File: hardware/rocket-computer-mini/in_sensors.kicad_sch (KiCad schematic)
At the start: 17 parts, among them J1 BM05B-SRSS-TB, U2 ISM6HG256XTR, U27 TPS22810DRVR, U3 IIS2MDCTR, U4 BMP585

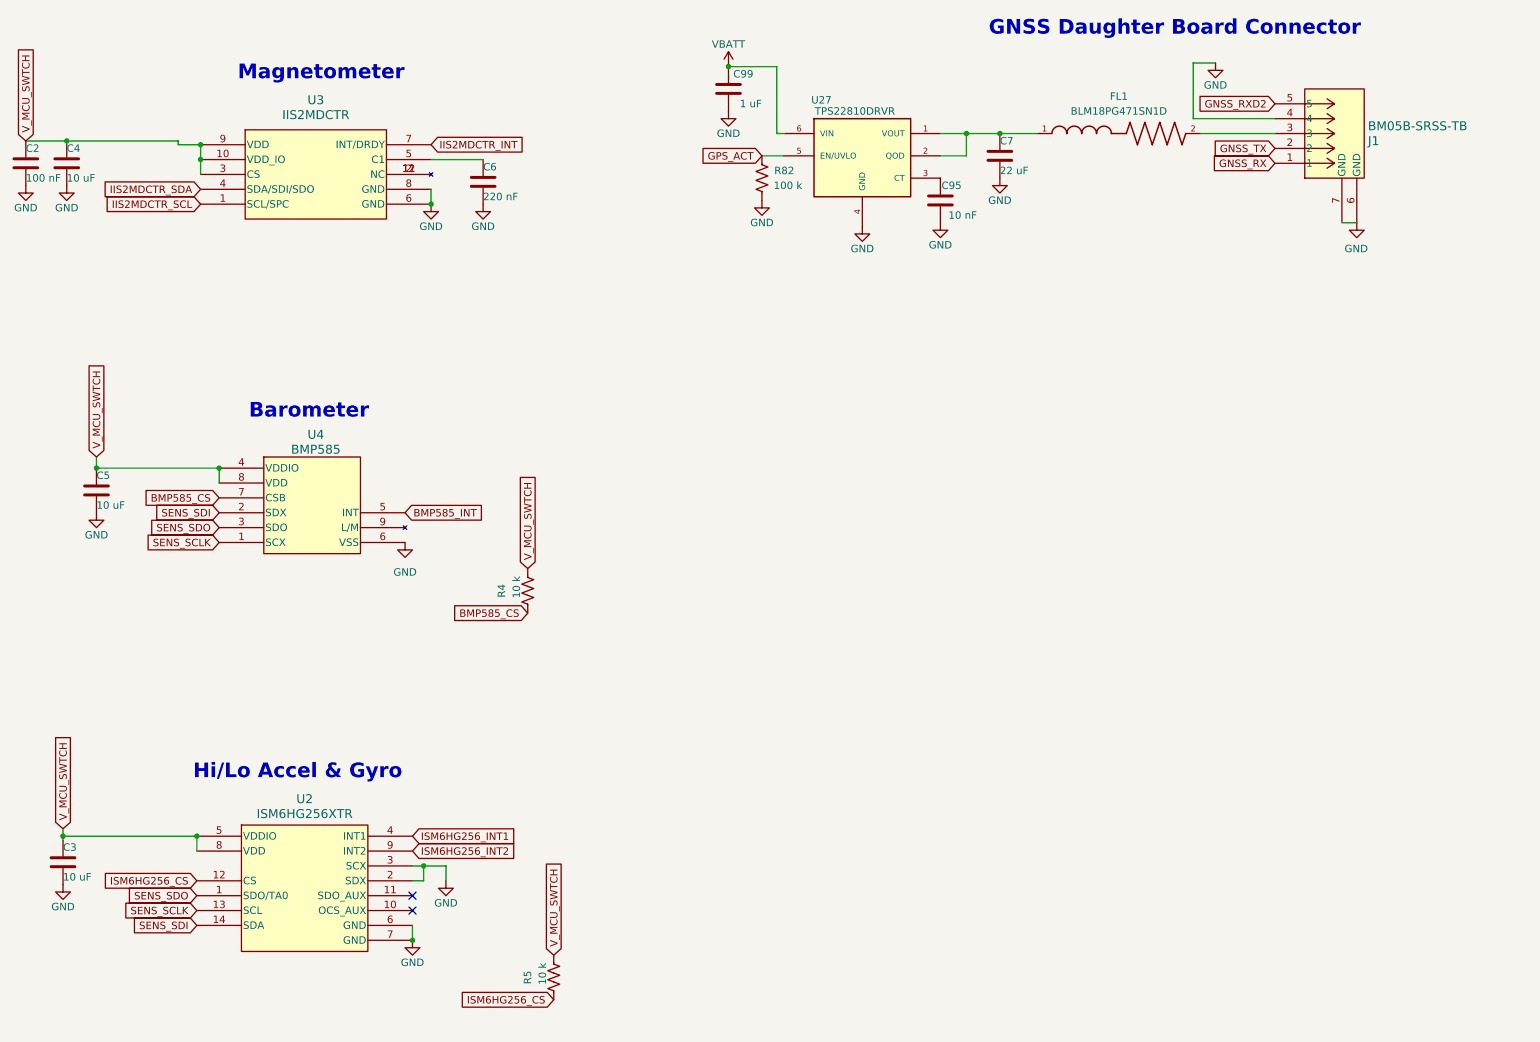
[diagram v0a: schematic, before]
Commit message: hardware: rocket-computer-mini gains the on-board radio, sheds more parts
Second reduction pass, plus the radio moves on-board.

Added: the 900 MHz radio module (U16) and its two decoupling caps, wired for
direct SPI rather than through the daughterboard connector. Removed: 31
designators including the camera connector (J4), the piezo (LS1), mounting
hardware (H5-H8), and the support parts that went with them. Also gone are the
magnetometer interrupt and the inertial sensor's second interrupt -- neither was
ever used by firmware, which is what made them free to drop.

Parts 190 -> 161, nets 191 -> 165.

Adds a pin budget for the reduced board (pin-budget.md). The headline is that
the board fits, but not comfortably: 23 signals against 27 usable pads, and only
16 of those pads are free of strapping, console, JTAG or flash-adjacent duty.

Three findings shaped it:

- The radio needs seven pins, not nine. DIO2 drives transmit-enable inside the
  module and needs no processor pin; receive-enable is floating and has no
  firmware pin at all. The out-computer firmware still carries the direct-SPI
  driver from the V7 topology and defines exactly those seven, so putting the
  bare module back on-board is a board change rather than a firmware rewrite.
- Pyro continuity is a digital read, not analogue, and nothing on this board
  needs an ADC channel -- so the ADC2-versus-radio restriction does not
  constrain the design.
- Continuity belongs on an I2C expander, not a multiplexer. A four-to-one mux
  needs two select lines plus data, saving one pin; the expander shares the bus
  the magnetometer is joining and saves four.

The proposed assignment keeps the serial console free and spends JTAG. Pyro
firing is confined to unrestricted pins -- never a strapping pin and never one
the boot ROM drives, since the console transmit pin is active on every boot.

One assumption can invalidate it: three signals sit on flash-adjacent pads that
are free only if the package carries no in-pa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
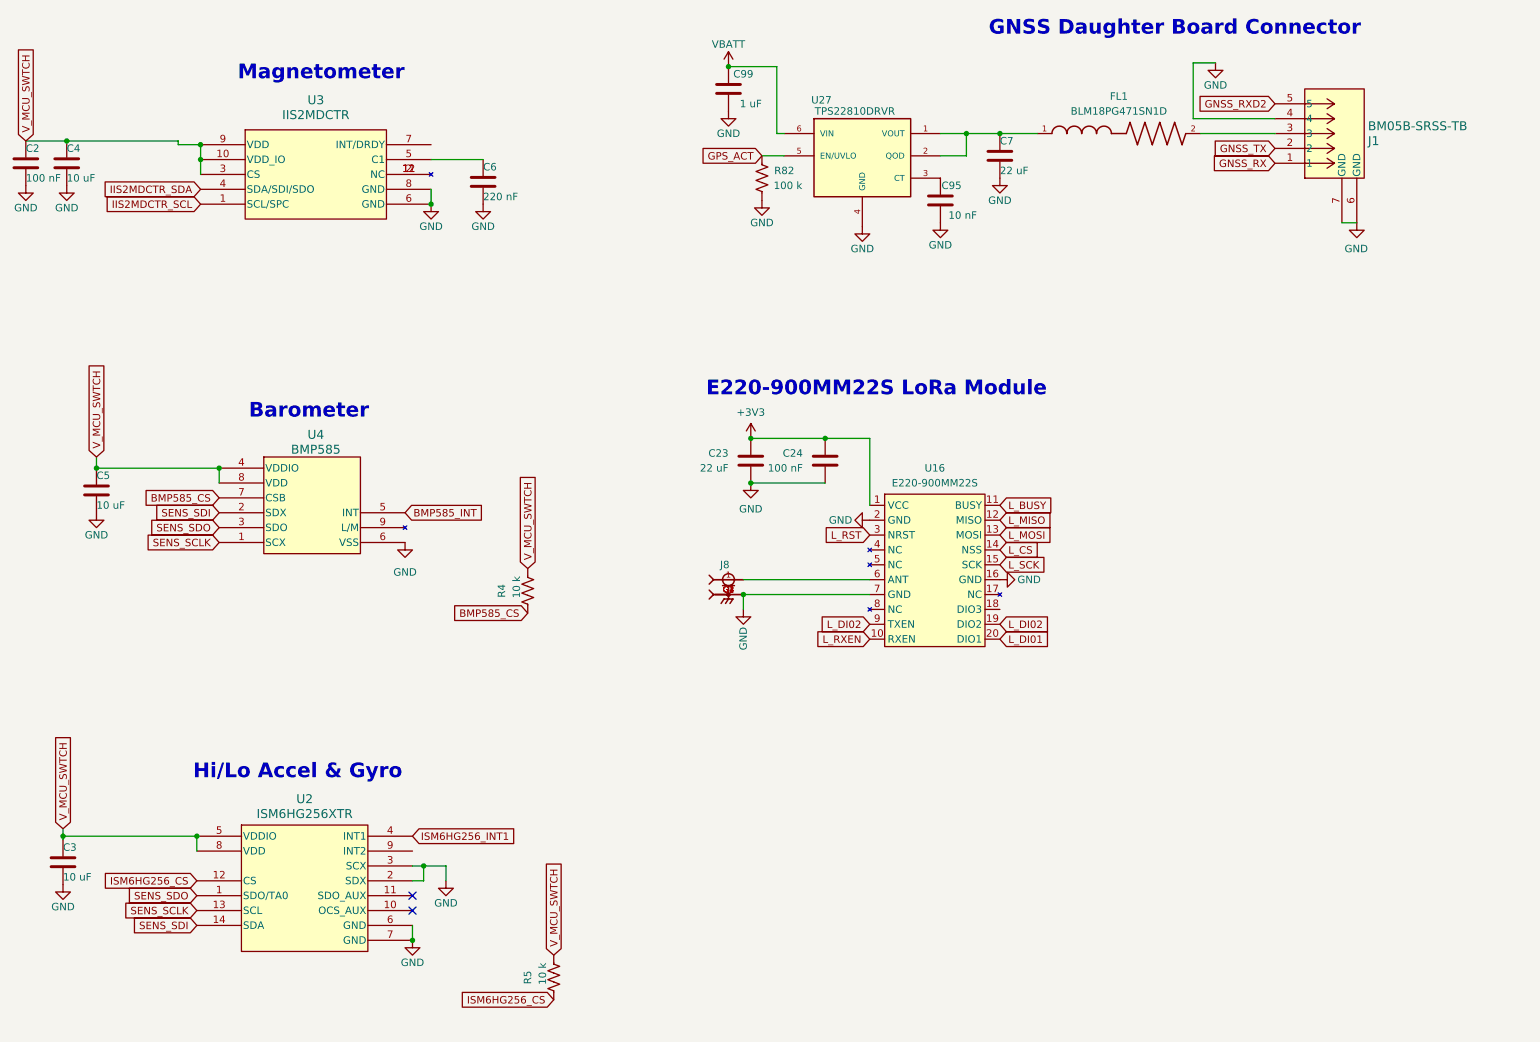
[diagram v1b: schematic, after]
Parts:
- added C23: 22 uF, Capacitor_SMD:C_0805_2012Metric, symbol Device:C
- added C24: 100 nF, Capacitor_SMD:C_0402_1005Metric, symbol Device:C
- added J8: CON-SMA-EDGE-S, Footprints:RFSOLUTIONS_CON-SMA-EDGE-S, symbol Custom:CON-SMA-EDGE-S
- added U16: E220-900MM22S, Footprints:E220-900MM22S, symbol Custom:E220-900MM22S
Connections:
- net GND: now also C23.1, C24.1, J8.G1, J8.G2, J8.G3, J8.G4, U16.16 (GND), U16.2 (GND), U16.7 (GND)
- net IIS2MDCTR_INT: no longer names the net of U3.7 (INT/DRDY)
- net ISM6HG256_INT2: no longer names the net of U2.9 (INT2)
- new net: J8.1, U16.6 (ANT)
- new net +3V3: C23.2, C24.2, U16.1 (VCC)
- new net L_BUSY: U16.11 (BUSY)
- new net L_CS: U16.14 (NSS)
- new net L_DI01: U16.20 (DIO1)
- new net L_DI02: U16.19 (DIO2), U16.9 (TXEN)
- new net L_MISO: U16.12 (MISO)
- new net L_MOSI: U16.13 (MOSI)
- new net L_RST: U16.3 (NRST)
- new net L_RXEN: U16.10 (RXEN)
- new net L_SCK: U16.15 (SCK)
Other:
- note added: "E220-900MM22S LoRa Module"

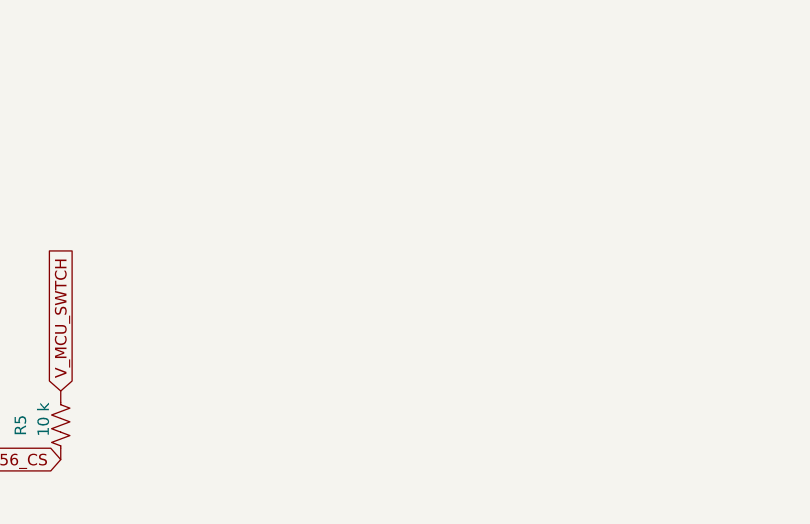
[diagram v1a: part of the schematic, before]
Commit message: hardware: place the LC86G GNSS module on rocket-computer-mini's sensors sheet
Brings in the GNSS symbol and footprint authored in the
lc86glamd-symbol-footprint-wiring worktree -- which had no commits of its own,
only uncommitted edits -- and places the part.

The symbol lands in the shared symbol library, so the addition was checked
before copying: 779 lines added, zero deleted, exactly one new top-level symbol
(248 -> 249), no collateral edits to any existing symbol. That library is shared
across every board in the repo and a careless import has damaged it before.

Placed as U5 on the Sensors sheet at (144.78, 170.18) -- the lowest free U
designator, and a position verified clear of every existing anchor by at least
2 mm with the symbol's full 35.6 x 35.6 mm extent, on the 1.27 mm grid.
Reference and value fields follow the library-to-instance Y flip; the remaining
fields are hidden at the origin, matching how the other sensor parts on this
sheet are drawn. Fields include MPN and Mfr per the BOM convention.

Placed, not wired. The pin assignment in pin-budget.md is a proposal, not a
decision, and wiring the module before that is settled would bake in a choice
that has not been made -- in particular whether the receiver keeps a branch
enable, which the budget drops to reach two pins.

Verified: the netlist exports cleanly with U5 on /Sensors/ carrying the right
value, footprint and datasheet; parts 161 -> 162. ERC goes 746 -> 758, and all
twelve new items are U5's own unconnected pins -- 8 pin_not_connected, 2
power_pin_not_driven, 2 pin_not_driven -- which is exactly what an unwired part
should produce and will clear as it is wired.

The footprint travels in the same commit as the board that uses it, per the
hardware README; a new part added without it breaks a clean clone.

Note for the power budget: this variant integrates its patch antenna and LNA,
so the external antenna bias left open there is not required.

Co-Authored-By: Claude Opus 5 <noreply@anthropic.co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
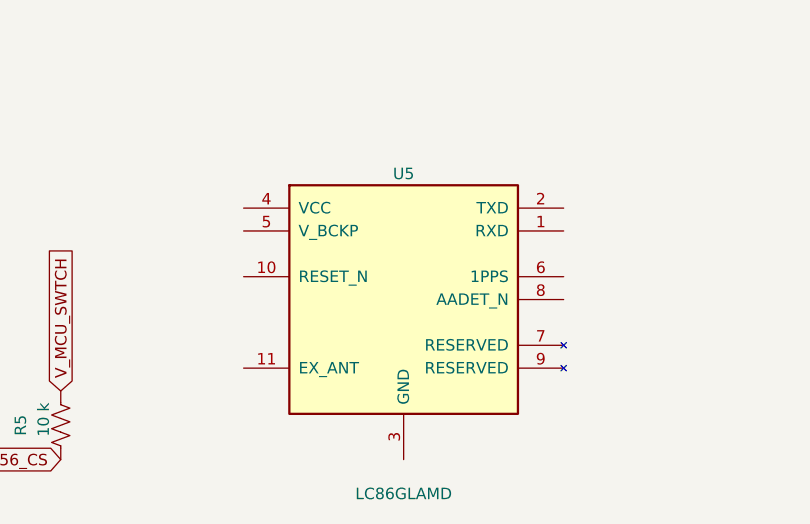
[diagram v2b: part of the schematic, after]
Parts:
- added U5: LC86GLAMD, Footprints:LC86GLAMD, symbol Custom:LC86GLAMD
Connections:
- net GND: now also U5.12 (GND), U5.13 (GND), U5.14 (GND), U5.15 (GND), U5.16 (GND), U5.17 (GND), U5.18 (GND), U5.19 (GND), U5.20 (GND), U5.21 (GND), U5.22 (GND), U5.23 (GND), U5.24 (GND), U5.25 (GND), U5.26 (GND), U5.27 (GND), U5.28 (GND), U5.29 (GND), U5.3 (GND), U5.30 (GND), U5.31 (GND), U5.32 (GND), U5.33 (GND), U5.34 (GND), U5.35 (GND), U5.36 (GND)
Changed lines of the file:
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@@
+		)
+	)
+	(symbol
+		(lib_id "Custom:LC86GLAMD")
+		(at 144.78 170.18 0)
+		(unit 1)
+		(body_style 1)
+		(exclude_from_sim no)
+		(in_bom yes)
+		(on_board yes)
+		(in_pos_files yes)
+		(dnp no)
+		(property "Reference" "U5"
+			(at 144.78 156.21 0)
+			(show_name no)
+			(effects
+				(font
+					(size 1.27 1.27)
+				)
+			)
+		)
+		(property "Value" "LC86GLAMD"
+			(at 144.78 191.77 0)
+			(show_name no)
+			(effects
+				(font
+					(size 1.27 1.27)
+				)
+			)
+		)
+		(property "Footprint" "Footprints:LC86GLAMD"
+			(at 144.78 170.18 0)
+			(hide yes)
+			(effects
+				(font
+					(size 1.27 1.27)
+				)
+			)
+		)
+		(property "Datasheet" "https://www.quectel.com/product/gnss-lc86g/"
+			(at 144.78 170.18 0)
+			(hide yes)
+			(effects
+				(font
+					(size 1.27 1.27)
+				)
+			)
+		)
+		(property "Description" ""
+			(at 144.78 170.18 0)
+			(hide yes)
+			(effects
+				(font
+					(size 1.27 1.27)
+				)
+			)
+		)
+		(property "MPN" "LC86GLAMD"
+			(at 144.78 170.18 0)
+			(hide yes)
+			(effects
+				(font
+					(size 1.27 1.27)
+				)
+			)
+		)
+		(property "Mfr" "Quectel"
+			(at 144.78 170.18 0)
+			(hide yes)
+			(effects
+				(font
+					(size 1.27 1.27)
+				)
+			)
+		)
+		(pin "4"
+		)
+		(pin "5"
+		)
+		(pin "10"
+		)
+		(pin "11"
+		)
+		(pin "2"
+		)
+		(pin "1"
+		)
+		(pin "6"
+		)
+		(pin "8"
+		)
+		(pin "7"
+		)
+		(pin "9"
+		)
+		(pin "3"
+		)
+		(pin "12"
+		)
+		(pin "13"
+		)
+		(pin "14"
+		)
+		(pin "15"
+		)
+		(pin "16"
+		)
+		(pin "17"
+		)
+		(pin "18"
+		)
+		(pin "19"
+		)
+		(pin "20"
+		)
+		(pin "21"
+		)
+		(pin "22"
+		)
+		(pin "23"
+		)
+		(pin "24"
+		)
+		(pin "25"
+		)
+		(pin "26"
+		)
+		(pin "27"
+		)
+		(pin "28"
+		)
+		(pin "29"
+		)
+		(pin "30"
+		)
+		(pin "31"
+		)
+		(pin "32"
+		)
+		(pin "33"
+		)
+		(pin "34"
+		)
+		(pin "35"
+		)
+		(pin "36"
+		)
+		(instances
+			(project "rocket-computer-mini"
+				(path "/ae61c2c4-72e9-4776-93ae-2e716b9dc70f/1c983e58-9603-45bc-a3c3-aa797d38a10d"
+					(reference "U5")
+					(unit 1)
+				)
+			)
 		)
 	)

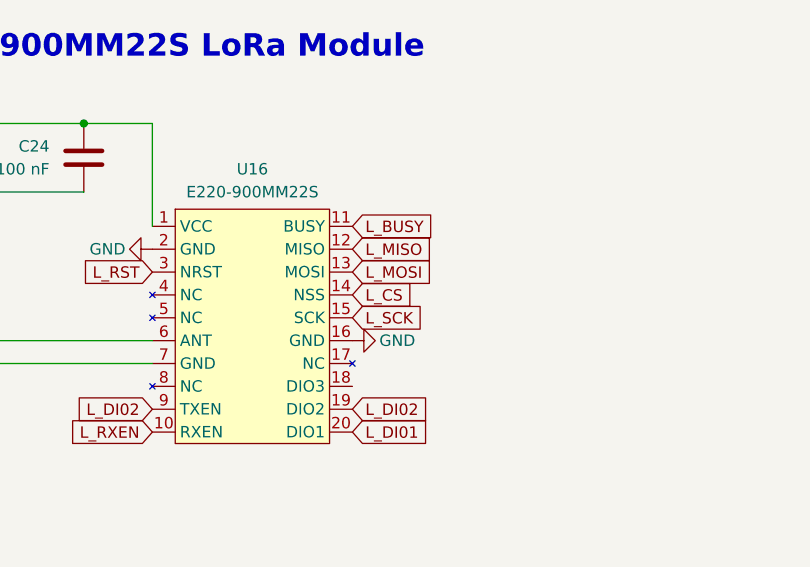
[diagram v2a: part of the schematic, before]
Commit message: hardware: radio joins the memory SPI bus, continuity sensing restored
Two changes that turned out to be the same change.

The radio moves onto the memory SPI bus -- clock, data-in and data-out shared
with the NAND, chip selects kept separate, which is what a bus is for. That
frees three processor pins for no new parts, and those pins go straight to pyro
continuity sensing, which until now reached nothing at all.

Continuity had been quietly lost. Those four nets went to the removed processor
and kept two nodes each -- a sense resistor and a clamp -- so they never showed
up in the single-endpoint sweep used to track what still needed rehoming. The
front end was intact the whole time; only the readout was missing. A board that
cannot check continuity can arm and fire into an open circuit and report nothing
wrong.

Which two devices share matters, and it is a latency question rather than a
bandwidth one -- there is large bandwidth margin either way. Memory moves in
page-sized bursts at 40 MHz that block the bus for hundreds of microseconds;
sensors are read per-sample on data-ready rather than batched through a FIFO, so
any bus delay lands directly as jitter on the sample timebase, and those samples
get integrated. The radio sends one small packet twice a second. Pairing memory
with the radio costs nothing; pairing it with the sensors would have put the
most latency-sensitive device behind the longest transactions.

This does split sensors and memory across hosts, which is not how the V7
firmware had them -- but this board has no firmware map yet, so the host
assignment is being written from scratch regardless.

The fourth continuity channel sits on GPIO44, spending the console receive line,
rather than the spare GPIO45. GPIO45 is sampled at reset to set the flash rail
voltage, and a continuity input's boot level depends on whether an igniter is
connected, which the design does not control -- an armed channel could hold that
pad high and stop the board booting. GPIO43 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
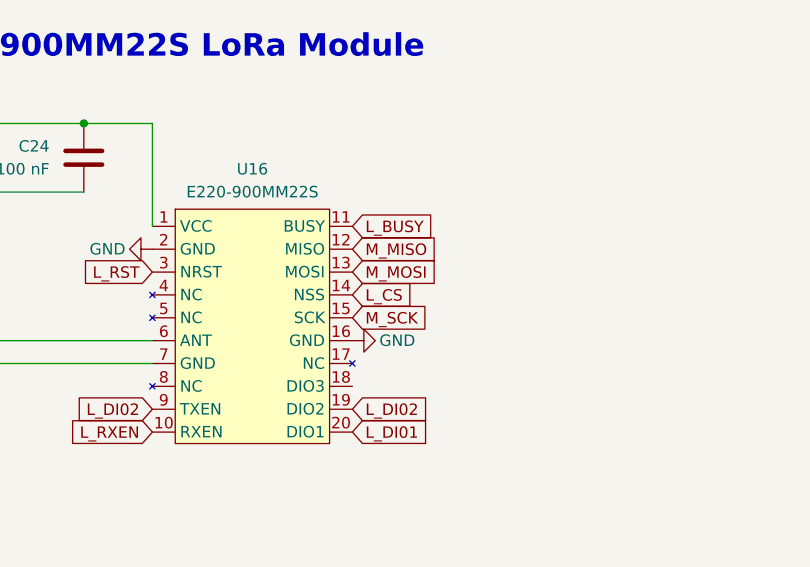
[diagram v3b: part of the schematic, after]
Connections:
- net L_MISO renamed M_MISO
- net L_MOSI renamed M_MOSI
- net L_SCK renamed M_SCK
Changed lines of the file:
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@@
 		)
 	)
-	(global_label "L_SCK"
+	(global_label "M_SCK"
 		(shape input)
 		(at 182.88 113.665 0)
@@
 		)
 	)
-	(global_label "L_MOSI"
+	(global_label "M_MOSI"
 		(shape input)
 		(at 182.88 108.585 0)
@@
 		)
 	)
-	(global_label "L_MISO"
+	(global_label "M_MISO"
 		(shape input)
 		(at 182.88 106.045 0)
